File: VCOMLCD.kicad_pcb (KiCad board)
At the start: 2 copper layers, 123.2 x 44.5 mm, 49 parts, among them J1 Screw_Terminal_01x02, J2 USB_B_Mini, J3 Conn_01x05, J4 Conn_01x03, J5 Conn_01x06, Q1 BC847, SW1 SYS_RST, SW2 BTN, U1 MCP73831-2-OT, U2 MCP1700-3302E_SOT23, U3 74LVC4245A, U4 LCD-016N002L, U5 STM32F042F4Px, U6 ESP-12E

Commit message: adding POC firmware
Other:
- net class Default removed
- net class PWR removed

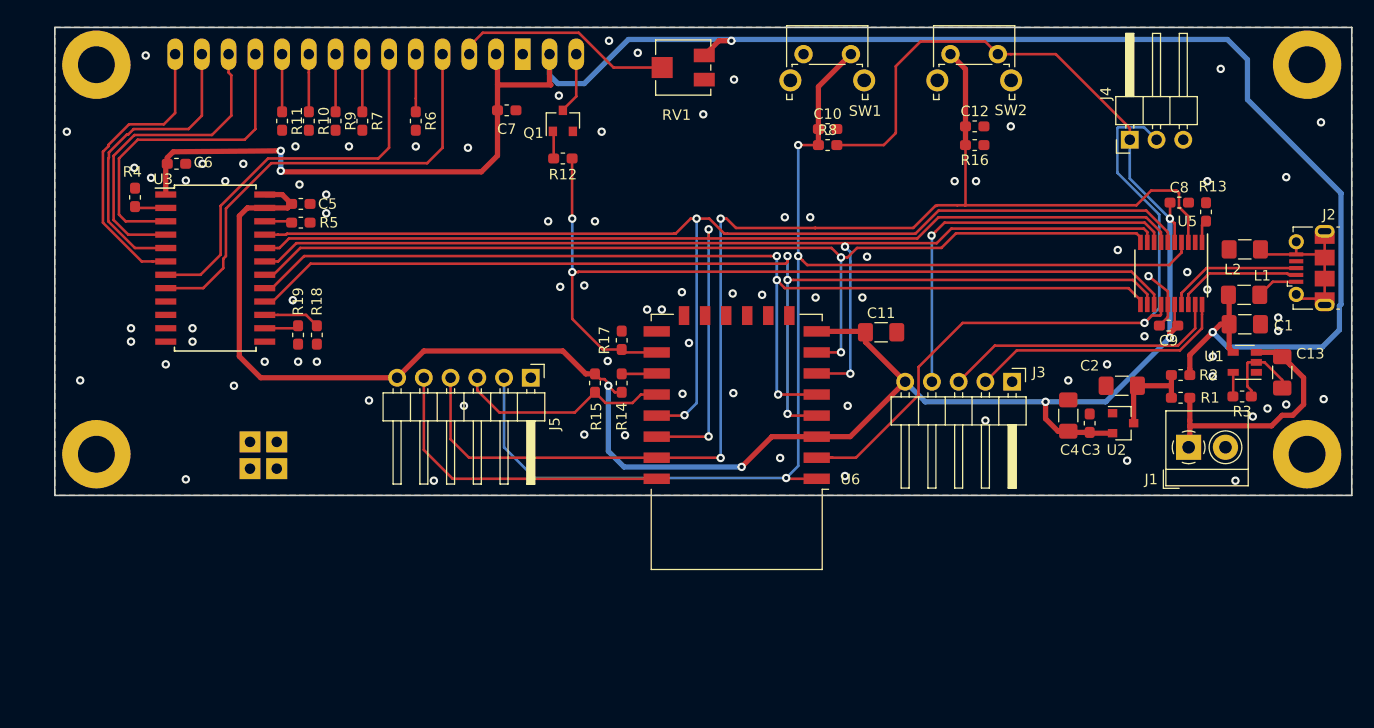
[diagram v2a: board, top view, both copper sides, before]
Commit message: work on new STM version - basic schematic and some of pcb
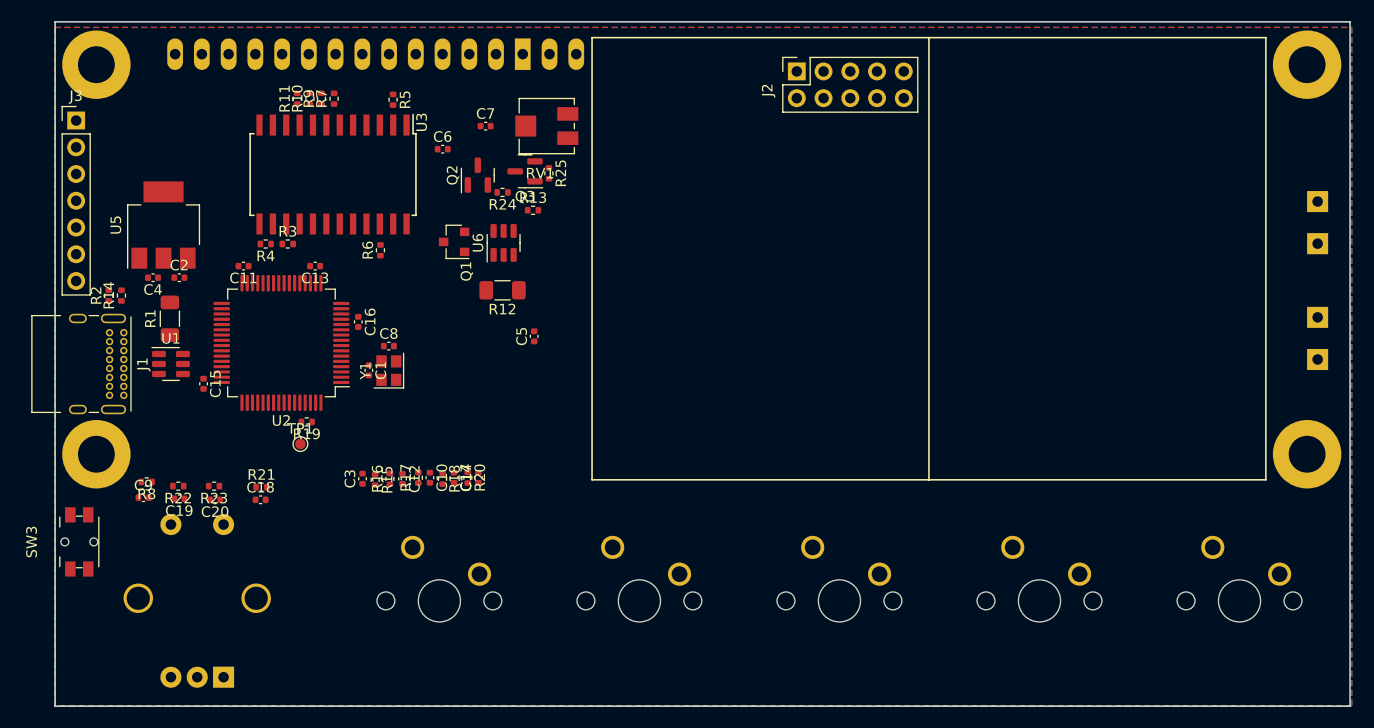
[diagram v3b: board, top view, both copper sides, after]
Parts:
- removed J4: Conn_01x03, Connector_PinHeader_2.54mm:PinHeader_1x03_P2.54mm_Horizontal
- removed J5: Conn_01x06, Connector_PinHeader_2.54mm:PinHeader_1x06_P2.54mm_Horizontal
- removed L1, L2: L_Small, Inductor_SMD:L_1206_3216Metric_Pad1.42x1.75mm_HandSolder
- added C14: 100n, Capacitor_SMD:C_0402_1005Metric, F.Cu at (115.4, 92.3)
- added C15: 100n, Capacitor_SMD:C_0402_1005Metric, F.Cu at (91.6, 83.4)
- added C16: 100n, Capacitor_SMD:C_0402_1005Metric, F.Cu at (106.3, 77.5)
- added C17: 100n, Capacitor_SMD:C_0402_1005Metric, F.Cu at (117.7, 92.3)
- added C18: 1n, Capacitor_SMD:C_0402_1005Metric, F.Cu at (97.0, 94.4)
- added C19: 1n, Capacitor_SMD:C_0402_1005Metric, F.Cu at (89.3, 94.3)
- added C20: 1n, Capacitor_SMD:C_0402_1005Metric, F.Cu at (92.7, 94.4)
- added Q2: AO3401A, Package_TO_SOT_SMD:SOT-23, F.Cu at (117.7, 63.6)
- added Q3: BC847, Package_TO_SOT_SMD:SOT-23, F.Cu at (122.1, 63.2)
- added R20: 10k, Resistor_SMD:R_0402_1005Metric, F.Cu at (116.7, 92.3)
- added R21: 100k, Resistor_SMD:R_0402_1005Metric, F.Cu at (97.1, 93.2)
- added R22: 100k, Resistor_SMD:R_0402_1005Metric, F.Cu at (89.2, 93.1)
- added R23: 100k, Resistor_SMD:R_0402_1005Metric, F.Cu at (92.6, 93.1)
- added R24: 10k, Resistor_SMD:R_0402_1005Metric, F.Cu at (120.0, 65.2)
- added R25: 3k, Resistor_SMD:R_0402_1005Metric, F.Cu at (124.4, 63.4)
- added SW3: BUT_SMD, Button_Switch_SMD:Panasonic_EVQPUM_EVQPUD, F.Cu at (79.8, 98.4)
- added SW4: BTN, Button_Switch_Keyboard:SW_Cherry_MX_1.00u_PCB, B.Cu at (149.5, 98.9)
- added SW5: BTN, Button_Switch_Keyboard:SW_Cherry_MX_1.00u_PCB, B.Cu at (130.5, 98.9)
- added SW6: BTN, Button_Switch_Keyboard:SW_Cherry_MX_1.00u_PCB, B.Cu at (111.5, 98.9)
- added SW7: RotaryEncoder_Switch, Rotary_Encoder:RotaryEncoder_Alps_EC12E-Switch_Vertical_H20mm_CircularMountingHoles, B.Cu at (93.5, 111.2)
- added TP1: STM_BOOT0, TestPoint:TestPoint_Pad_D1.0mm, F.Cu at (100.8, 89.1)
- added Y1: 6MHZ 2520, Crystal:Crystal_SMD_2520-4Pin_2.5x2.0mm, F.Cu at (109.2, 82.1)
- C1: value 22u -> 20p; footprint Capacitor_SMD:C_1206_3216Metric_Pad1.42x1.75mm_HandSolder -> Capacitor_SMD:C_0402_1005Metric
- C10, C12, C3, C5, C6, C7: footprint Capacitor_SMD:C_0603_1608Metric_Pad1.05x0.95mm_HandSolder -> Capacitor_SMD:C_0402_1005Metric
- C11, C13: value 22u -> 100n; footprint Capacitor_SMD:C_1206_3216Metric_Pad1.42x1.75mm_HandSolder -> Capacitor_SMD:C_0402_1005Metric
- C2, C4: value 22u -> 10u; footprint Capacitor_SMD:C_1206_3216Metric_Pad1.42x1.75mm_HandSolder -> Capacitor_SMD:C_0402_1005Metric
- C8: value 100n -> 20p; footprint Capacitor_SMD:C_0603_1608Metric_Pad1.05x0.95mm_HandSolder -> Capacitor_SMD:C_0402_1005Metric
- C9: value 100n -> 1n; footprint Capacitor_SMD:C_0603_1608Metric_Pad1.05x0.95mm_HandSolder -> Capacitor_SMD:C_0402_1005Metric
- J1: value Screw_Terminal_01x02 -> USB_C_Receptacle_USB2.0; footprint TerminalBlock_4Ucon:TerminalBlock_4Ucon_1x02_P3.50mm_Horizontal -> Connector_USB:USB_C_Receptacle_GCT_USB4085
- J2: value USB_B_Mini -> EXT_MOD_CONN; footprint Connector_USB:USB_Micro-B_Molex-105017-0001 -> Connector_PinSocket_2.54mm:PinSocket_2x05_P2.54mm_Vertical
- J3: value Conn_01x05 -> Conn_01x07; footprint Connector_PinHeader_2.54mm:PinHeader_1x05_P2.54mm_Horizontal -> Connector_PinHeader_2.54mm:PinHeader_1x07_P2.54mm_Vertical
- R1: value NC -> 0R/1206; footprint Resistor_SMD:R_0603_1608Metric_Pad1.05x0.95mm_HandSolder -> Resistor_SMD:R_1206_3216Metric_Pad1.30x1.75mm_HandSolder
- R10, R11, R14, R17, R4, R5, R6, R7, R9: footprint Resistor_SMD:R_0603_1608Metric_Pad1.05x0.95mm_HandSolder -> Resistor_SMD:R_0402_1005Metric
- R12: value R -> 0.1R; footprint Resistor_SMD:R_0603_1608Metric_Pad1.05x0.95mm_HandSolder -> Resistor_SMD:R_1206_3216Metric_Pad1.30x1.75mm_HandSolder
- R13, R16, R3: value R -> 10k; footprint Resistor_SMD:R_0603_1608Metric_Pad1.05x0.95mm_HandSolder -> Resistor_SMD:R_0402_1005Metric
- R15, R18, R19: value NC -> 10k; footprint Resistor_SMD:R_0603_1608Metric_Pad1.05x0.95mm_HandSolder -> Resistor_SMD:R_0402_1005Metric
- R2: value 0R -> 10k; footprint Resistor_SMD:R_0603_1608Metric_Pad1.05x0.95mm_HandSolder -> Resistor_SMD:R_0402_1005Metric
- R8: value R -> 100k; footprint Resistor_SMD:R_0603_1608Metric_Pad1.05x0.95mm_HandSolder -> Resistor_SMD:R_0402_1005Metric
- SW1: value SYS_RST -> BTN; footprint Button_Switch_THT:SW_Tactile_SPST_Angled_PTS645Vx83-2LFS -> Button_Switch_Keyboard:SW_Cherry_MX_1.00u_PCB; moved to B.Cu
- SW2: footprint Button_Switch_THT:SW_Tactile_SPST_Angled_PTS645Vx83-2LFS -> Button_Switch_Keyboard:SW_Cherry_MX_1.00u_PCB; moved to B.Cu
- U1: value MCP73831-2-OT -> USBLC6-2SC6; footprint Package_TO_SOT_SMD:SOT-23-5 -> Package_TO_SOT_SMD:SOT-23-6
- U2: value MCP1700-3302E_SOT23 -> STM32F103RFTx; footprint Package_TO_SOT_SMD:SOT-23 -> Package_QFP:LQFP-64_10x10mm_P0.5mm
- U5: value STM32F042F4Px -> AMS1117-3.3; footprint Package_SO:TSSOP-20_4.4x6.5mm_P0.65mm -> Package_TO_SOT_SMD:SOT-223-3_TabPin2
- U6: value ESP-12E -> INA181; footprint RF_Module:ESP-12E -> Package_TO_SOT_SMD:SOT-23-6
- moved R2 102.1 mm to (82.6, 75.0), turned to 90 degrees
- moved U1 102.0 mm to (88.5, 81.5), turned to 0 degrees
- moved J1 101.7 mm to (84.0, 78.5), turned to -90 degrees
- moved C9 98.7 mm to (85.9, 94.2), turned to 0 degrees
- moved R1 96.3 mm to (88.4, 77.2), turned to 90 degrees
- moved U5 95.8 mm to (87.8, 68.3), turned to 90 degrees
- moved C13 92.4 mm to (102.2, 72.2), turned to 180 degrees
- moved J3 92.3 mm to (79.5, 58.4), turned to 0 degrees
- moved R3 91.8 mm to (99.6, 70.1), turned to 0 degrees
- moved C2 90.1 mm to (89.3, 73.3), turned to 0 degrees
- moved C4 87.9 mm to (86.8, 73.3), turned to 180 degrees
- moved C1 83.3 mm to (107.3, 82.1), turned to -90 degrees
- moved U2 80.3 mm to (99.0, 79.5), turned to 180 degrees
- moved C8 76.3 mm to (109.2, 79.8)
- moved R8 72.2 mm to (86.2, 92.7), turned to 180 degrees
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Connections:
- C1 pad 1: VBUS -> Net-(U2-Pad5)
- C10 pad 1: /ESP_RTS -> /BTN3
- C11 pad 1: +3V3 -> GND
- C11 pad 2: GND -> +3V3
- C12 pad 1: /BTN -> /BTN1
- C13 pad 1: +BATT -> GND
- C13 pad 2: GND -> +3V3
- C2 pad 1: Net-(C2-Pad1) -> VBUS
- C3 pad 1: +3V3 -> /BTN2
- C8 pad 1: +3V3 -> Net-(U2-Pad6)
- C9 pad 1: +3V3 -> Net-(U2-Pad7)
- J2 pad 1: Net-(J2-Pad1) -> /STM32_CLK
- J2 pad 2: Net-(J2-Pad2) -> /STM32_CS
- J2 pad 3: Net-(J2-Pad3) -> GND
- J2 pad 4: Net-(J2-Pad4) -> VDD
- J2 pad 5: Net-(J2-Pad5) -> /STM32_MISO
- J2 pad 6: Net-(J2-Pad5) -> /STM32_SDA
- J3 pad 1: GND -> +3V3
- J3 pad 2: /SWCLK -> /STM_TX
- J3 pad 3: /SWDIO -> /STM_RX
- J3 pad 4: /STM_TX -> GND
- J3 pad 5: +3V3 -> /SWDIO
- Q1 pad 2: GND -> Net-(Q1-Pad2)
- R1 pad 1: Net-(C2-Pad1) -> Net-(J1-PadA4)
- R1 pad 2: +BATT -> VBUS
- R10 pad 1: Net-(R10-Pad1) -> GND
- R10 pad 2: GND -> Net-(U4-Pad9)
- R11 pad 1: Net-(R11-Pad1) -> GND
- R11 pad 2: GND -> Net-(U4-Pad10)
- R12 pad 1: Net-(Q1-Pad1) -> GND
- R12 pad 2: /BL_CTRL -> Net-(Q1-Pad2)
- R13 pad 1: GND -> /BL_CTRL
- R13 pad 2: Net-(R13-Pad2) -> Net-(Q1-Pad1)
- R14 pad 1: Net-(R14-Pad1) -> Net-(J1-PadA5)
- R14 pad 2: +3V3 -> GND
- R15 pad 1: /ESP_DTR -> GND
- R15 pad 2: +3V3 -> /BTN2
- R16 pad 2: /BTN -> /BTN1
- R17 pad 2: /BL_CTRL -> /BTN3
- R18 pad 2: Net-(R18-Pad2) -> /BTN4
- R19 pad 2: Net-(R19-Pad2) -> Net-(U2-Pad60)
- R2 pad 1: Net-(C2-Pad1) -> GND
- R2 pad 2: VBUS -> Net-(J1-PadB5)
- R3 pad 2: Net-(R3-Pad2) -> Net-(U3-Pad15)
- R4 pad 1: GND -> Net-(U3-Pad14)
- R4 pad 2: Net-(R4-Pad2) -> GND
- R5 pad 2: Net-(R5-Pad2) -> Net-(U3-Pad2)
- R6 pad 1: Net-(R6-Pad1) -> Net-(U3-Pad22)
- R7 pad 1: Net-(R7-Pad1) -> GND
- R7 pad 2: GND -> Net-(U4-Pad7)
- R8 pad 1: /ESP_RTS -> Net-(U2-Pad7)
- R9 pad 1: Net-(R9-Pad1) -> GND
- R9 pad 2: GND -> Net-(U4-Pad8)
- SW1 pad 1: GND -> /BTN2
- SW1 pad 2: /ESP_RTS -> +3V3
- SW2 pad 1: /BTN -> /BTN1
- U1 pad 1: Net-(U1-Pad1) -> Net-(J1-PadA7)
- U1 pad 3: +BATT -> Net-(J1-PadA6)
- U1 pad 4: VBUS -> /USB_DP
- U1 pad 5: Net-(R3-Pad2) -> Net-(J1-PadA4)
- U2 pad 1: GND -> +3V3
- U2 pad 2: +3V3 -> unconnected-(U2-Pad2)
- U2 pad 3: Net-(C2-Pad1) -> unconnected-(U2-Pad3)
- U3 pad 10: Net-(U3-Pad10) -> unconnected-(U3-Pad10)
- U3 pad 14: Net-(R19-Pad2) -> Net-(U3-Pad14)
- U3 pad 15: Net-(R18-Pad2) -> Net-(U3-Pad15)
- U3 pad 16: Net-(U3-Pad16) -> /DISP_RS
- U3 pad 17: Net-(U3-Pad17) -> /DISP_E
- U3 pad 18: Net-(U3-Pad18) -> /DISP_DB7
- U3 pad 19: Net-(U3-Pad19) -> /DISP_DB6
- U3 pad 2: Net-(R4-Pad2) -> Net-(U3-Pad2)
- U3 pad 20: Net-(U3-Pad20) -> /DISP_DB5
- U3 pad 21: Net-(U3-Pad21) -> /DISP_DB4
- U3 pad 22: Net-(R5-Pad2) -> Net-(U3-Pad22)
- U3 pad 9: Net-(U3-Pad9) -> unconnected-(U3-Pad9)
- U4 pad 10: Net-(R11-Pad1) -> Net-(U4-Pad10)
- U4 pad 5: Net-(R6-Pad1) -> GND
- U4 pad 7: Net-(R7-Pad1) -> Net-(U4-Pad7)
- U4 pad 8: Net-(R9-Pad1) -> Net-(U4-Pad8)
- U4 pad 9: Net-(R10-Pad1) -> Net-(U4-Pad9)
- U4 pad A1: Net-(U4-PadA1) -> unconnected-(U4-PadA1)
- U4 pad A2: Net-(U4-PadA2) -> unconnected-(U4-PadA2)
- U4 pad K1: Net-(U4-PadK1) -> unconnected-(U4-PadK1)
- U4 pad K2: Net-(U4-PadK2) -> unconnected-(U4-PadK2)
- U5 pad 1: Net-(R13-Pad2) -> GND
- U5 pad 2: Net-(U5-Pad2) -> +3V3
- U5 pad 3: /BTN -> VBUS
- U6 pad 1: /ESP_RTS -> /BL_CURR_MEAS
- U6 pad 2: Net-(J4-Pad2) -> GND
- U6 pad 3: +3V3 -> Net-(Q1-Pad2)
- U6 pad 4: Net-(U3-Pad16) -> GND
- U6 pad 5: Net-(U3-Pad17) -> GND
- U6 pad 6: Net-(U3-Pad19) -> +3V3
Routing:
- net +3V3: track 216.9 -> 0.00 mm, vias 5 -> 0
- net VBUS: track 185.2 -> 0.00 mm, vias 4 -> 0
- net /BTN: track 120.6 -> 0.00 mm, vias 2 -> 0
- net /ESP_RTS: track 119.7 -> 0.00 mm, vias 3 -> 0
- net Net-(U3-Pad20): track 113.4 -> 0.00 mm, vias 2 -> 0
- net Net-(U3-Pad21): track 111.5 -> 0.00 mm, vias 2 -> 0
- net Net-(U3-Pad16): track 105.3 -> 0.00 mm, vias 3 -> 0
- net Net-(U3-Pad17): track 102.5 -> 0.00 mm, vias 3 -> 0
- net Net-(U3-Pad19): track 102.2 -> 0.00 mm, vias 2 -> 0
- net Net-(U3-Pad18): track 97.5 -> 0.00 mm, vias 2 -> 0
- net /BL_CTRL: track 81.7 -> 0.00 mm, vias 2 -> 0
- net Net-(J4-Pad2): track 67.3 -> 0.00 mm, vias 1 -> 0
- net Net-(U3-Pad8): track 44.9 -> 0.00 mm
- net Net-(U3-Pad7): track 38.3 -> 0.00 mm
- net /STM_TX: track 36.9 -> 0.00 mm, vias 1 -> 0
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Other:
- board size 123.2 x 44.5 mm -> 123 x 65 mm
